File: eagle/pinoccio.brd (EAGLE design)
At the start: 25.4 x 50.8 mm, 60 parts, among them IC1 ATMEGA16U2QFN32, J1 AVR_SPI_PRG_6, Q1 16MHz, Q2 32.768k, Q3 16MHz, U1 MCP73831, U2 TPS78233, U4 ATMEGA128RFA1, X1 USB-MICROB, Y2 ANTENNA2SMD5

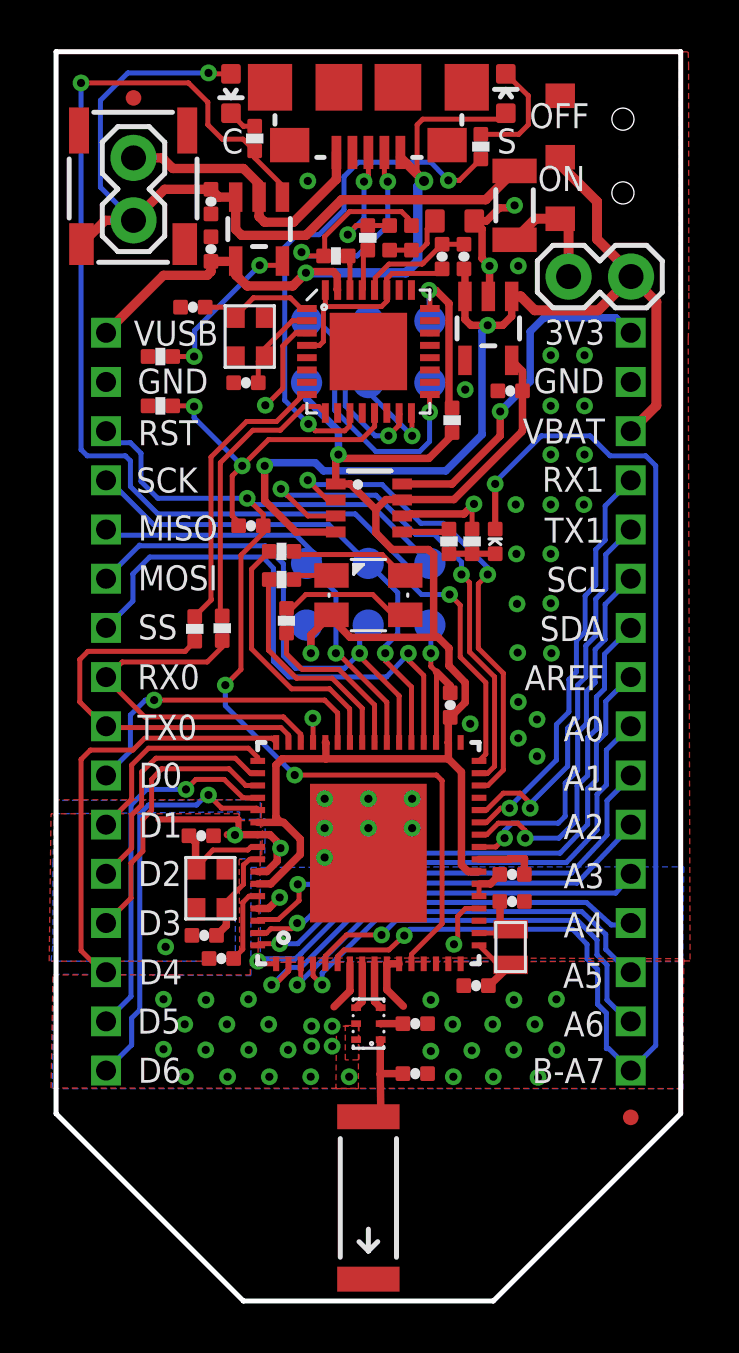
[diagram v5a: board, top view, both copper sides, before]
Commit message: Adjust a couple of spacing issues
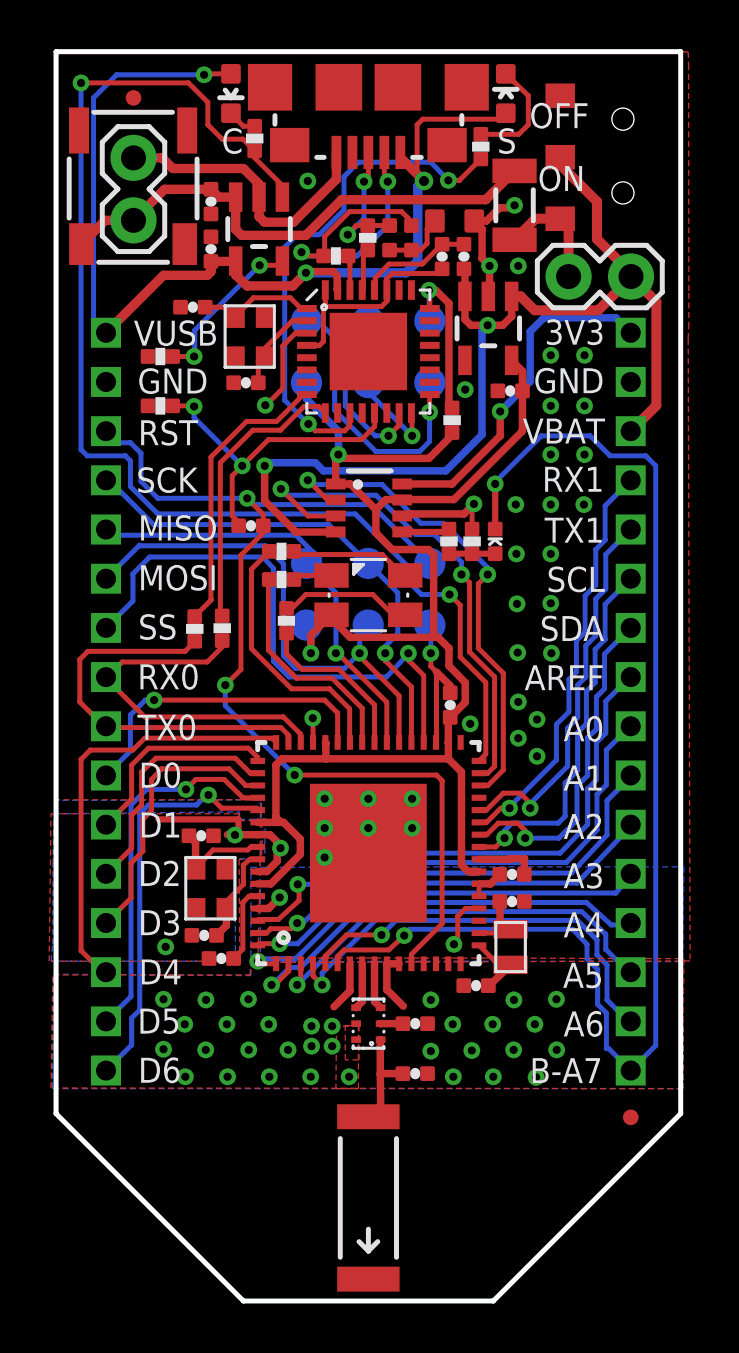
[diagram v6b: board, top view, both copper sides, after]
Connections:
- net VBAT: no longer D2.A
- net VUSB: now also D2.A
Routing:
- net VUSB: track 28.4 -> 44.2 mm, vias 2 -> 3
- net VBAT: track 32.4 -> 21.2 mm, vias 1 -> 0
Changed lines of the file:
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@@
 <text x="3.362" y="12.873" size="1.016" layer="21" font="vector" ratio="15">D4</text>
 <text x="3.3112" y="10.873" size="1.016" layer="21" font="vector" ratio="15">D5</text>
-<text x="22.3301" y="9.8762" size="1.016" layer="21" font="vector" ratio="15" rot="R180">B-A7</text>
+<text x="22.2285" y="9.8762" size="1.016" layer="21" font="vector" ratio="15" rot="R180">B-A7</text>
 <text x="22.292" y="11.7746" size="1.016" layer="21" font="vector" ratio="15" rot="R180">A6</text>
 <text x="22.2666" y="13.7492" size="1.016" layer="21" font="vector" ratio="15" rot="R180">A5</text>
@@
 <via x="18.796" y="42.0878" extent="1-16" drill="0.3302"/>
 <via x="17.6276" y="42.0878" extent="1-16" drill="0.3302"/>
-<via x="19.5978" y="9.0932" extent="1-16" drill="0.3302"/>
+<via x="19.5216" y="9.0932" extent="1-16" drill="0.3302"/>
 <via x="17.78" y="9.1186" extent="1-16" drill="0.3302"/>
 <via x="19.4708" y="11.2522" extent="1-16" drill="0.3302"/>
@@
 <wire x1="6.1468" y1="41.7068" x2="4.3688" y2="41.7068" width="0.381" layer="1"/>
 <wire x1="4.3688" y1="41.7068" x2="2.032" y2="39.37" width="0.381" layer="1"/>
+<wire x1="6.0578" y1="49.8982" x2="6.0198" y2="49.8602" width="0.2032" layer="1"/>
+<via x="6.0198" y="49.8602" extent="1-16" drill="0.3302"/>
+<wire x1="6.0198" y1="49.8602" x2="2.4638" y2="49.8602" width="0.2032" layer="16"/>
+<wire x1="2.4638" y1="49.8602" x2="1.524" y2="48.9204" width="0.2032" layer="16"/>
+<wire x1="1.524" y1="48.9204" x2="1.524" y2="39.878" width="0.2032" layer="16"/>
+<wire x1="1.524" y1="39.878" x2="2.032" y2="39.37" width="0.2032" layer="16"/>
 <wire x1="14.9606" y1="45.5422" x2="14.6812" y2="45.8216" width="0.2032" layer="1"/>
 <wire x1="14.6812" y1="45.8216" x2="14.6812" y2="47.8282" width="0.2032" layer="1"/>
@@
 <contactref element="U1" pad="4"/>
 <contactref element="U1" pad="4"/>
+<contactref element="D2" pad="A"/>
+<wire x1="6.0578" y1="49.8982" x2="7.112" y2="49.8982" width="0.2032" layer="1"/>
 <wire x1="7.305" y1="42.2863" x2="7.3152" y2="42.2761" width="0" layer="19" extent="1-1"/>
 <wire x1="6.9875" y1="42.2736" x2="7.3152" y2="42.2761" width="0" layer="19" extent="1-1"/>
@@
 <wire x1="10.16" y1="43.3324" x2="11.6078" y2="44.7802" width="0.381" layer="1"/>
 <wire x1="11.6078" y1="44.7802" x2="17.4722" y2="44.7802" width="0.381" layer="1"/>
-<contactref element="D2" pad="A"/>
-<wire x1="7.112" y1="49.8982" x2="6.2358" y2="49.8982" width="0.2032" layer="1"/>
-<wire x1="6.2358" y1="49.8982" x2="6.1976" y2="49.9364" width="0.2032" layer="1"/>
-<via x="6.1976" y="49.9364" extent="1-16" drill="0.3302"/>
-<wire x1="6.1976" y1="49.9364" x2="2.921" y2="49.9364" width="0.2032" layer="16"/>
-<wire x1="2.921" y1="49.9364" x2="1.8034" y2="48.8188" width="0.2032" layer="16"/>
-<wire x1="1.8034" y1="48.8188" x2="1.8034" y2="45.2882" width="0.2032" layer="16"/>
-<wire x1="1.8034" y1="45.2882" x2="3.1496" y2="43.942" width="0.2032" layer="16"/>
 </signal>
 <signal name="VBAT-AE">
